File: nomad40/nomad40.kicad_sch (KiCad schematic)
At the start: 2 parts

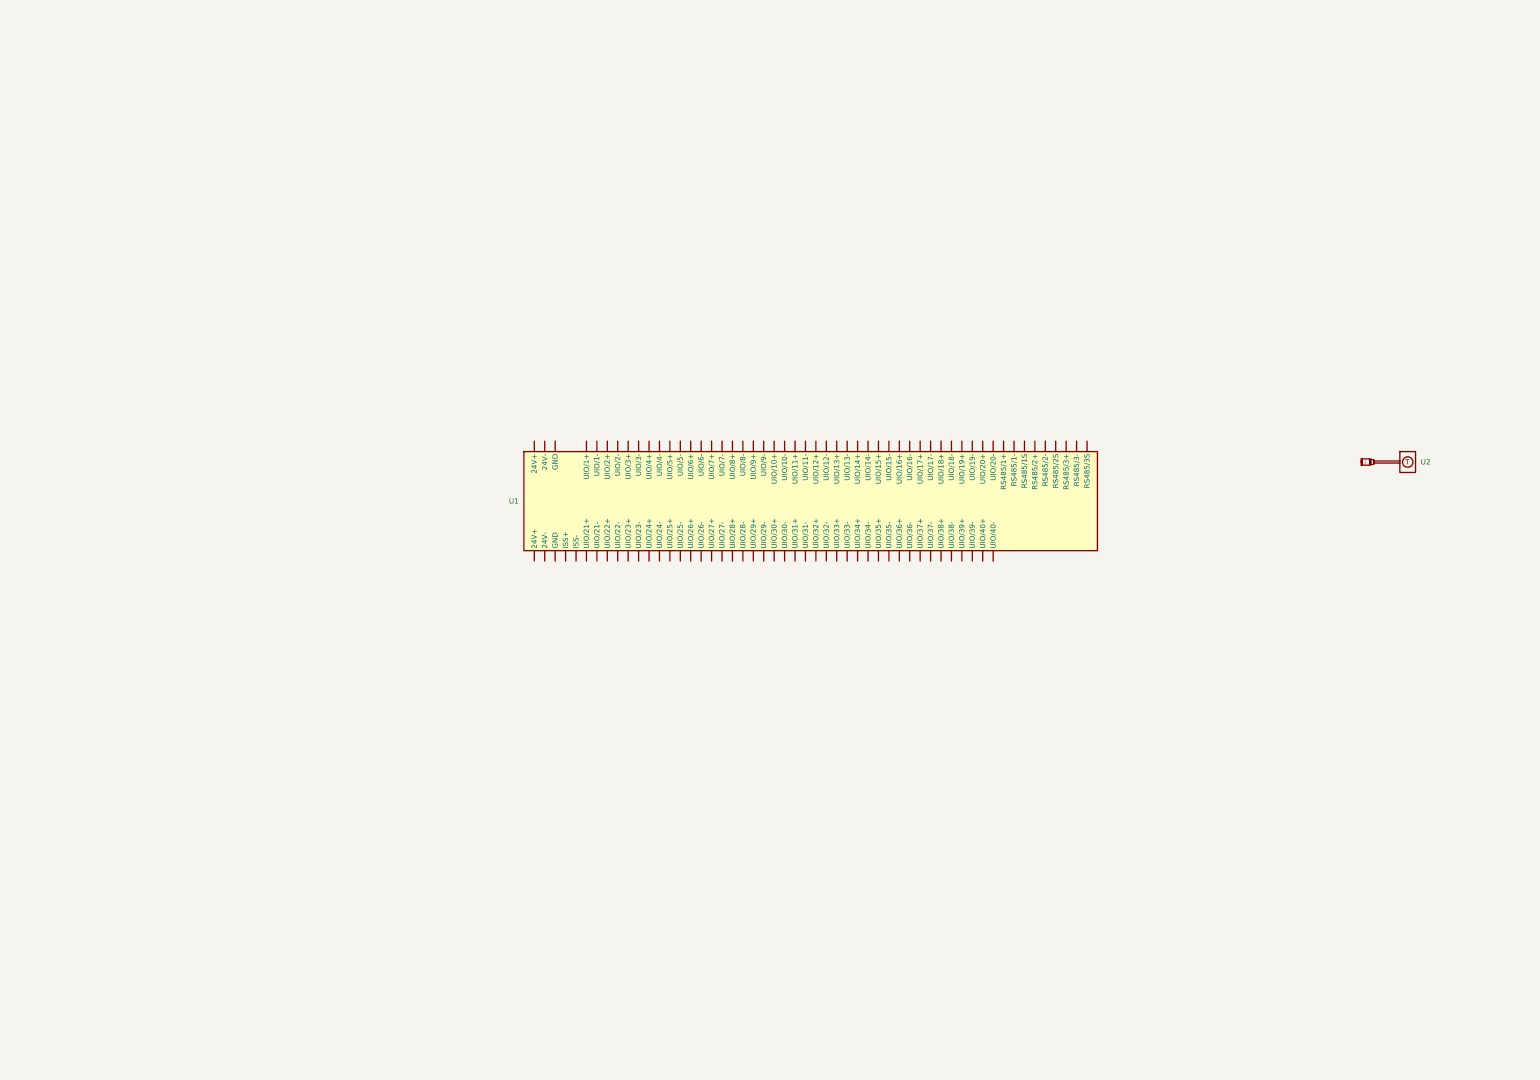
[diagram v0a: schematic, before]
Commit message: tank 1-4 schematics
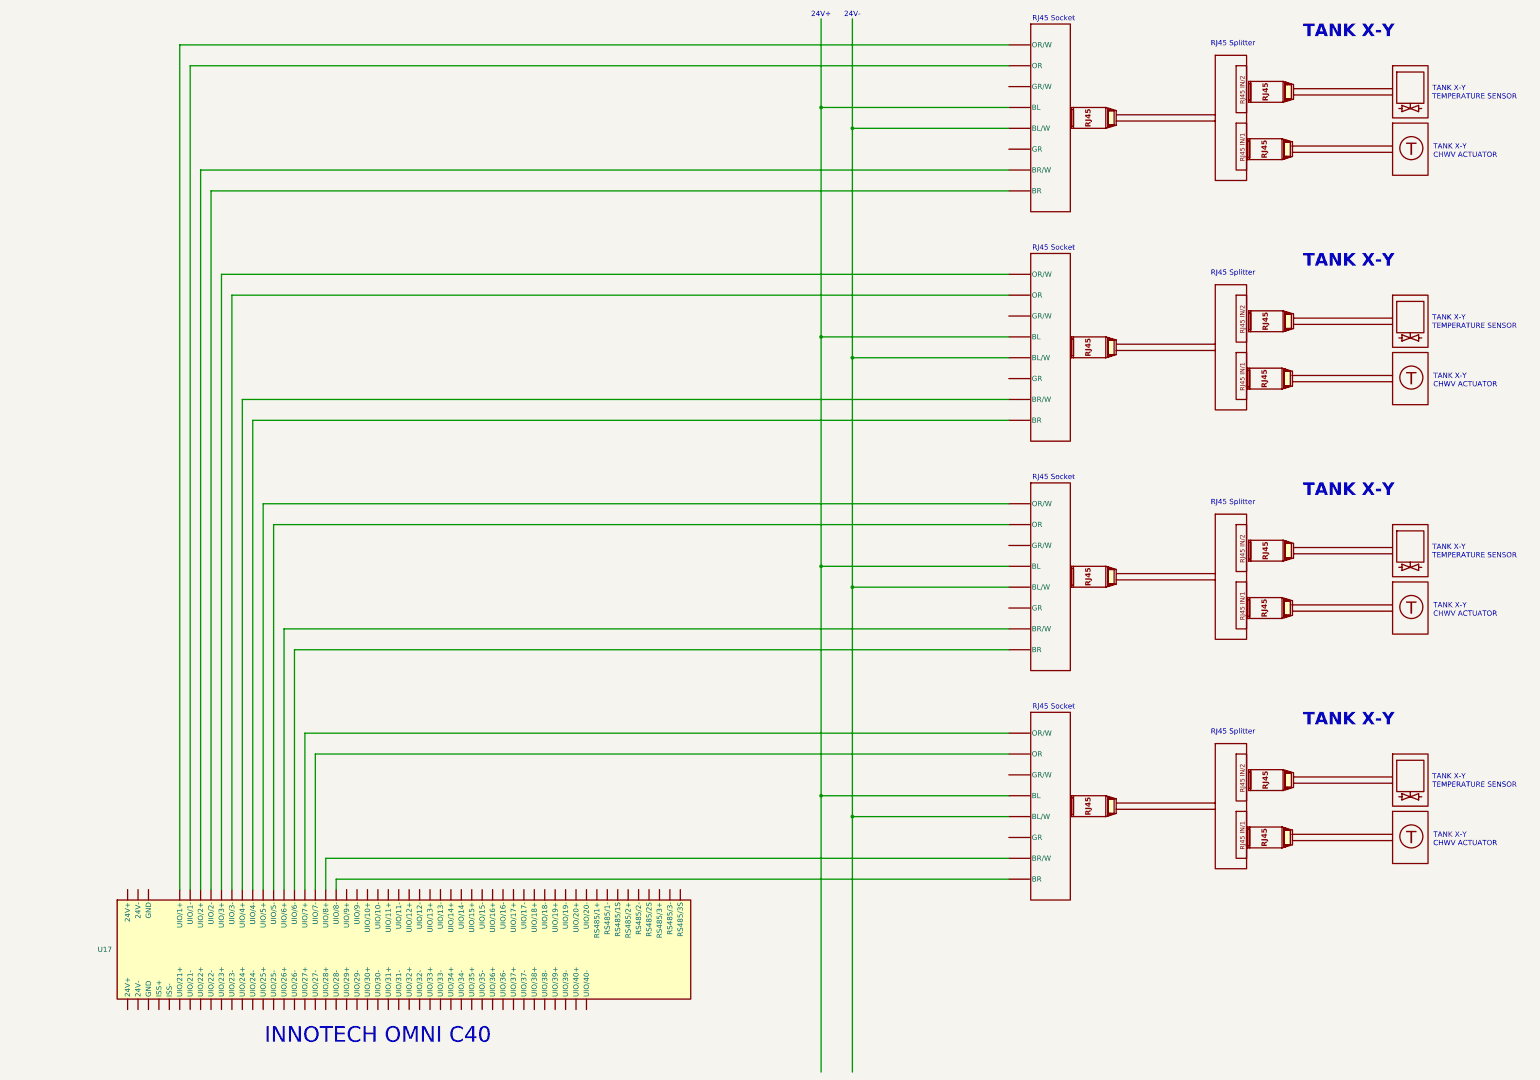
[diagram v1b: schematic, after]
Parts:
- removed U1: (no value), symbol Innotech:Omni_C40
- added U1, U13, U15, U7: (no value), symbol Innotech:Chilled_Water_Valve
- added U10, U4, U5, U9: (no value), symbol Innotech:RJ45_Socket
- added U11, U12, U3, U6: (no value), symbol Innotech:RJ45_Breakout
- added U14, U16, U8: (no value), symbol Innotech:Temperature_Sensor
- added U17: (no value), symbol Innotech:Omni_C40
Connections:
- new net: U17. (RS485/3S), U9. (BR) (x4)
- new net: U10. (BR), U4. (BR), U5. (BR), U9. (BR) (x2)
- new net: U17. (RS485/3S), U4. (BR) (x4)
- new net: U17. (RS485/3S), U5. (BR) (x4)
- new net: U10. (BR), U17. (RS485/3S) (x4)
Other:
- note added: "24V+"
- note added: "24V-"
- note added: "INNOTECH OMNI C40"
- note added: "RJ45 Socket"
- note added: "RJ45 Splitter"
- note added: "TANK X-Y"
- note added: "TANK X-Y CHWV ACTUATOR"
- note added: "TANK X-Y TEMPERATURE SENSOR"

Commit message: create hierarchical sheet
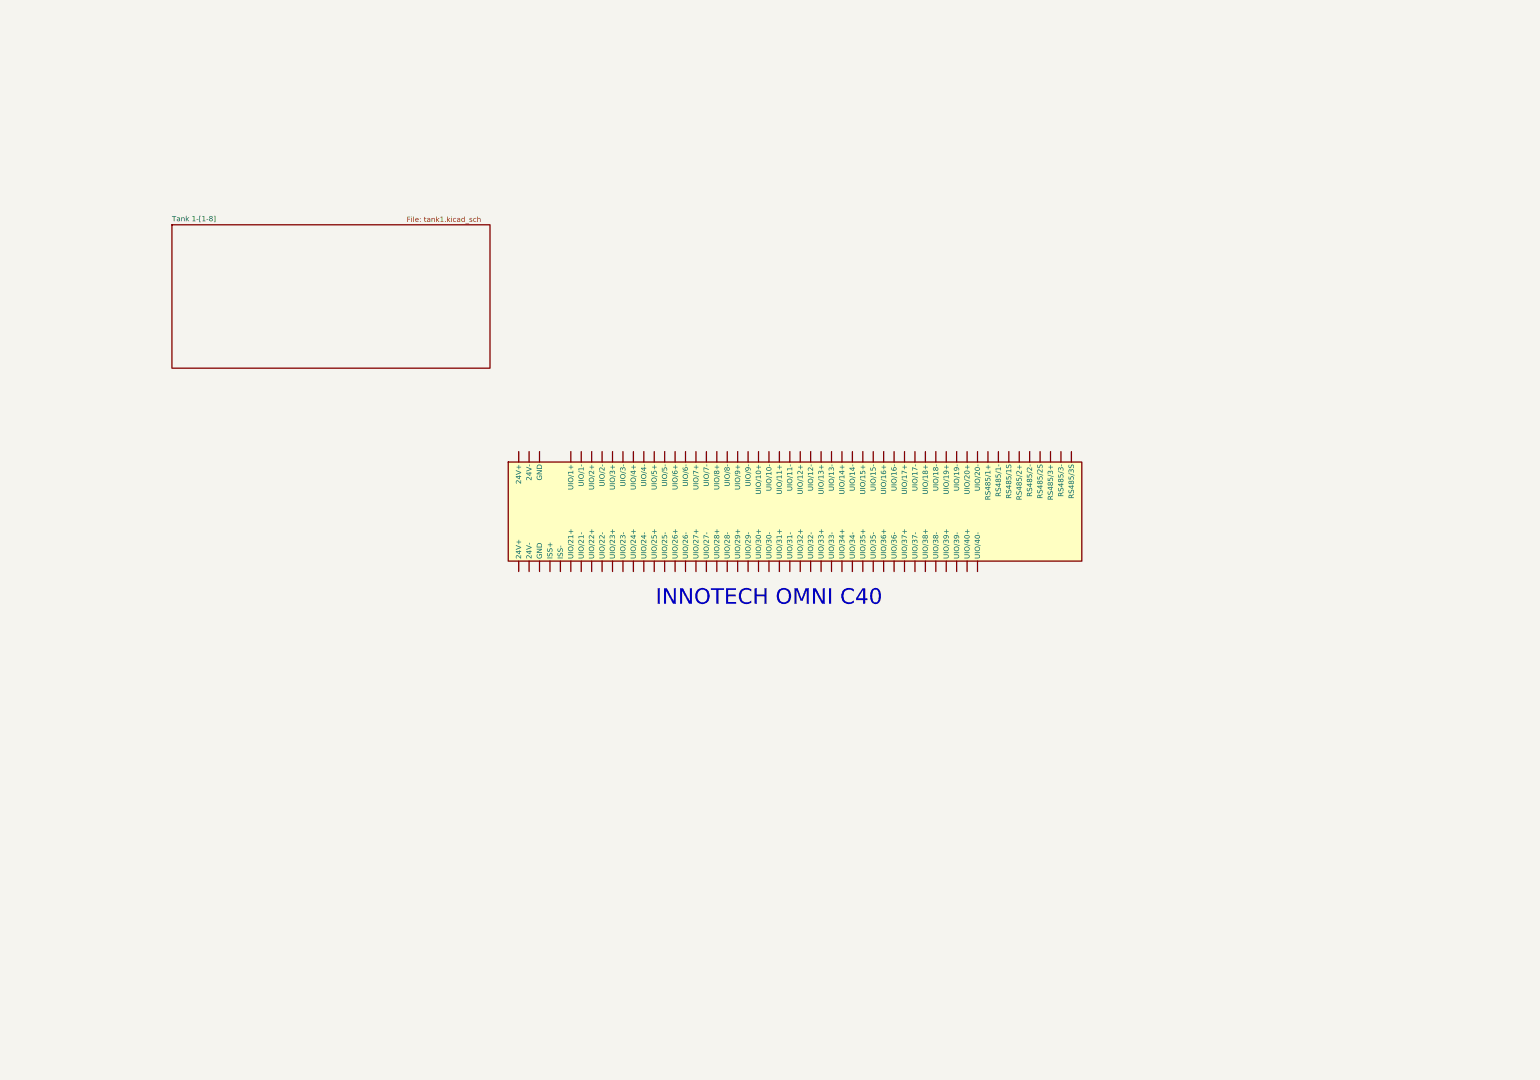
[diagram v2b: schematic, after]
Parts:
- removed U1, U13, U15, U7: (no value), symbol Innotech:Chilled_Water_Valve
- removed U10, U4, U5, U9: (no value), symbol Innotech:RJ45_Socket
- removed U11, U12, U3, U6: (no value), symbol Innotech:RJ45_Breakout
- removed U14, U16, U2, U8: (no value), symbol Innotech:Temperature_Sensor
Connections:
- now unconnected: U17. (RS485/3S), U17. (RS485/3S), U17. (RS485/3S), U17. (RS485/3S), U17. (RS485/3S), U17. (RS485/3S), U17. (RS485/3S), U17. (RS485/3S), U17. (RS485/3S), U17. (RS485/3S), U17. (RS485/3S), U17. (RS485/3S), U17. (RS485/3S), U17. (RS485/3S), U17. (RS485/3S)
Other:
- added sheet Tank 1-[1-8] (tank1.kicad_sch)
- note removed: "24V+"
- note removed: "24V-"
- note removed: "RJ45 Socket"
- note removed: "RJ45 Splitter"
- note removed: "TANK X-Y"
- note removed: "TANK X-Y CHWV ACTUATOR"
- note removed: "TANK X-Y TEMPERATURE SENSOR"

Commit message: add tank2-[1-8] sheet
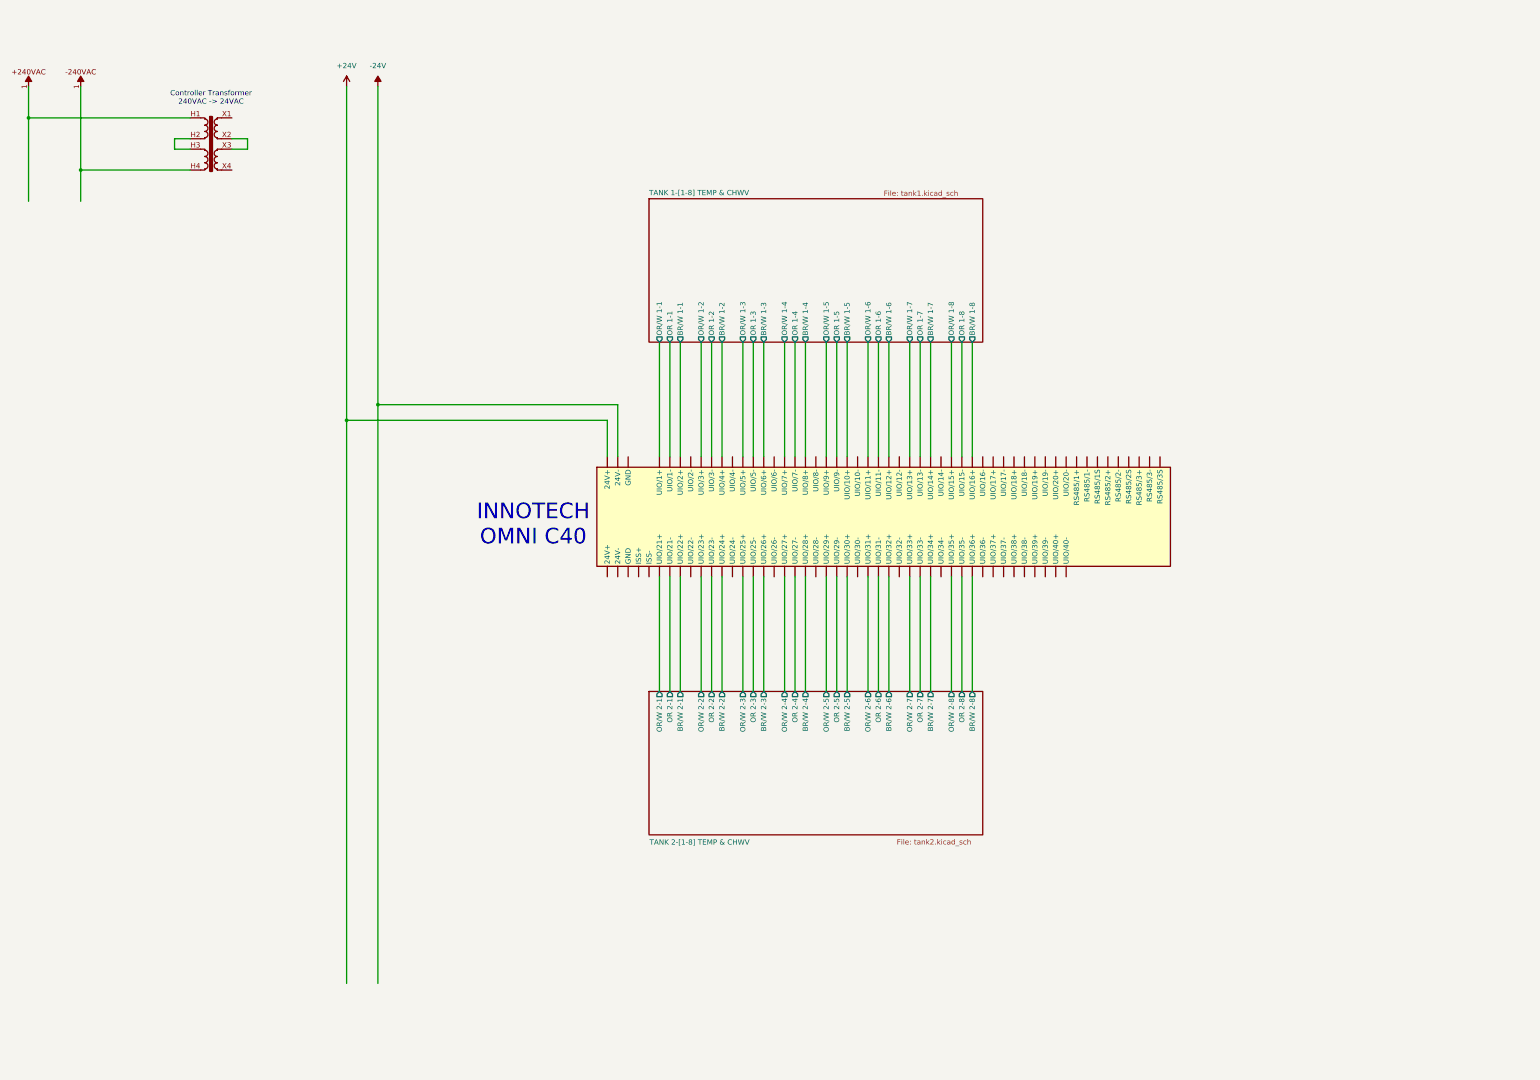
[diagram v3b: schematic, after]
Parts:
- added U114: (no value), symbol Innotech:24VAC_Transformer
- added U115: (no value), symbol Innotech:+240VAC
- added U116: (no value), symbol Innotech:-240VAC
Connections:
- net TANK 2-[1-8] TEMP & CHWV/OR/W 2-8: now reaches U17. (RS485/3S)
- new net: U114.H1, U115.1
- new net: U114.H2, U114.H3
- new net: U114.H4, U116.1
- new net: U114.X2, U114.X3
- new net +24V: U17. (RS485/3S)
- new net -24V: U17. (RS485/3S)
- new net TANK 1-[1-8] TEMP & CHWV/BR/W 1-1: U17. (RS485/3S)
- new net TANK 1-[1-8] TEMP & CHWV/BR/W 1-2: U17. (RS485/3S)
- new net TANK 1-[1-8] TEMP & CHWV/BR/W 1-3: U17. (RS485/3S)
- new net TANK 1-[1-8] TEMP & CHWV/BR/W 1-4: U17. (RS485/3S)
- new net TANK 1-[1-8] TEMP & CHWV/BR/W 1-5: U17. (RS485/3S)
- new net TANK 1-[1-8] TEMP & CHWV/BR/W 1-6: U17. (RS485/3S)
- new net TANK 1-[1-8] TEMP & CHWV/BR/W 1-7: U17. (RS485/3S)
- new net TANK 1-[1-8] TEMP & CHWV/BR/W 1-8: U17. (RS485/3S)
- new net TANK 1-[1-8] TEMP & CHWV/OR 1-1: U17. (RS485/3S)
- new net TANK 1-[1-8] TEMP & CHWV/OR 1-2: U17. (RS485/3S)
- new net TANK 1-[1-8] TEMP & CHWV/OR 1-3: U17. (RS485/3S)
- new net TANK 1-[1-8] TEMP & CHWV/OR 1-4: U17. (RS485/3S)
- new net TANK 1-[1-8] TEMP & CHWV/OR 1-5: U17. (RS485/3S)
- new net TANK 1-[1-8] TEMP & CHWV/OR 1-6: U17. (RS485/3S)
- new net TANK 1-[1-8] TEMP & CHWV/OR 1-7: U17. (RS485/3S)
- new net TANK 1-[1-8] TEMP & CHWV/OR 1-8: U17. (RS485/3S)
- new net TANK 1-[1-8] TEMP & CHWV/OR/W 1-1: U17. (RS485/3S)
- new net TANK 1-[1-8] TEMP & CHWV/OR/W 1-2: U17. (RS485/3S)
- new net TANK 1-[1-8] TEMP & CHWV/OR/W 1-3: U17. (RS485/3S)
- new net TANK 1-[1-8] TEMP & CHWV/OR/W 1-4: U17. (RS485/3S)
- new net TANK 1-[1-8] TEMP & CHWV/OR/W 1-5: U17. (RS485/3S)
- new net TANK 1-[1-8] TEMP & CHWV/OR/W 1-6: U17. (RS485/3S)
- new net TANK 1-[1-8] TEMP & CHWV/OR/W 1-7: U17. (RS485/3S)
- new net TANK 1-[1-8] TEMP & CHWV/OR/W 1-8: U17. (RS485/3S)
- new net TANK 2-[1-8] TEMP & CHWV/BR/W 2-1: U17. (RS485/3S)
- new net TANK 2-[1-8] TEMP & CHWV/BR/W 2-2: U17. (RS485/3S)
- new net TANK 2-[1-8] TEMP & CHWV/BR/W 2-3: U17. (RS485/3S)
- new net TANK 2-[1-8] TEMP & CHWV/BR/W 2-4: U17. (RS485/3S)
- new net TANK 2-[1-8] TEMP & CHWV/BR/W 2-5: U17. (RS485/3S)
- new net TANK 2-[1-8] TEMP & CHWV/BR/W 2-6: U17. (RS485/3S)
- new net TANK 2-[1-8] TEMP & CHWV/BR/W 2-7: U17. (RS485/3S)
- new net TANK 2-[1-8] TEMP & CHWV/BR/W 2-8: U17. (RS485/3S)
- new net TANK 2-[1-8] TEMP & CHWV/OR 2-1: U17. (RS485/3S)
- new net TANK 2-[1-8] TEMP & CHWV/OR 2-2: U17. (RS485/3S)
- new net TANK 2-[1-8] TEMP & CHWV/OR 2-3: U17. (RS485/3S)
- new net TANK 2-[1-8] TEMP & CHWV/OR 2-4: U17. (RS485/3S)
- new net TANK 2-[1-8] TEMP & CHWV/OR 2-5: U17. (RS485/3S)
- new net TANK 2-[1-8] TEMP & CHWV/OR 2-6: U17. (RS485/3S)
- new net TANK 2-[1-8] TEMP & CHWV/OR 2-7: U17. (RS485/3S)
- new net TANK 2-[1-8] TEMP & CHWV/OR 2-8: U17. (RS485/3S)
- new net TANK 2-[1-8] TEMP & CHWV/OR/W 2-1: U17. (RS485/3S)
- new net TANK 2-[1-8] TEMP & CHWV/OR/W 2-2: U17. (RS485/3S)
- new net TANK 2-[1-8] TEMP & CHWV/OR/W 2-3: U17. (RS485/3S)
- new net TANK 2-[1-8] TEMP & CHWV/OR/W 2-4: U17. (RS485/3S)
- new net TANK 2-[1-8] TEMP & CHWV/OR/W 2-5: U17. (RS485/3S)
- new net TANK 2-[1-8] TEMP & CHWV/OR/W 2-6: U17. (RS485/3S)
- new net TANK 2-[1-8] TEMP & CHWV/OR/W 2-7: U17. (RS485/3S)
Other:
- sheet Tank 1-[1-8] renamed TANK 1-[1-8] TEMP & CHWV
- added sheet TANK 2-[1-8] TEMP & CHWV (tank2.kicad_sch)
- sheet TANK 1-[1-8] TEMP & CHWV ports: added BR/W 1-1, BR/W 1-2, BR/W 1-3, BR/W 1-4, BR/W 1-5, BR/W 1-6, BR/W 1-7, BR/W 1-8, OR 1-1, OR 1-2, OR 1-3, OR 1-4, OR 1-5, OR 1-6, OR 1-7, OR 1-8, OR/W 1-1, OR/W 1-2, OR/W 1-3, OR/W 1-4, OR/W 1-5, OR/W 1-6, OR/W 1-7, OR/W 1-8; removed none
- note added: "Controller Transformer 240VAC -> 24VAC"
